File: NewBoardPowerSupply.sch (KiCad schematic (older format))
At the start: 22 parts, among them IC201 ADM7172ACPZ-4.2-R7, IC202 LT1716CS5#TRPBF, IC203 ADM7154ARDZ-3.3-R7, IC204 IRF9358PBF, U201 LM4040EIM3X-2.5_NOPB

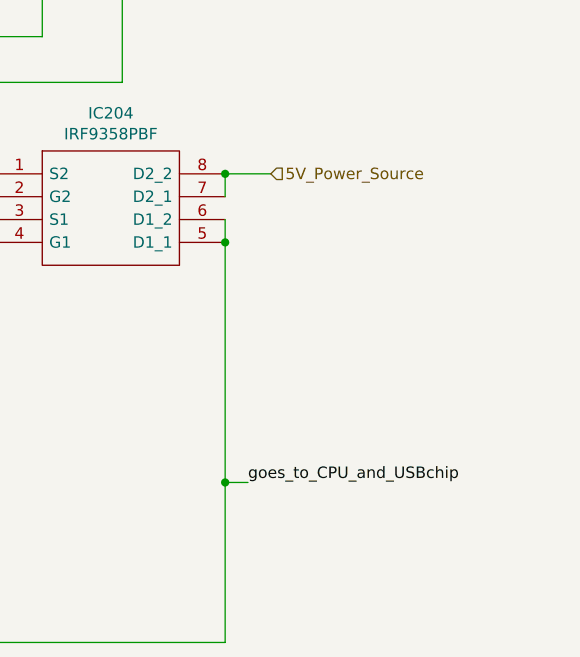
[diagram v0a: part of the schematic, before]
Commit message: added other ports
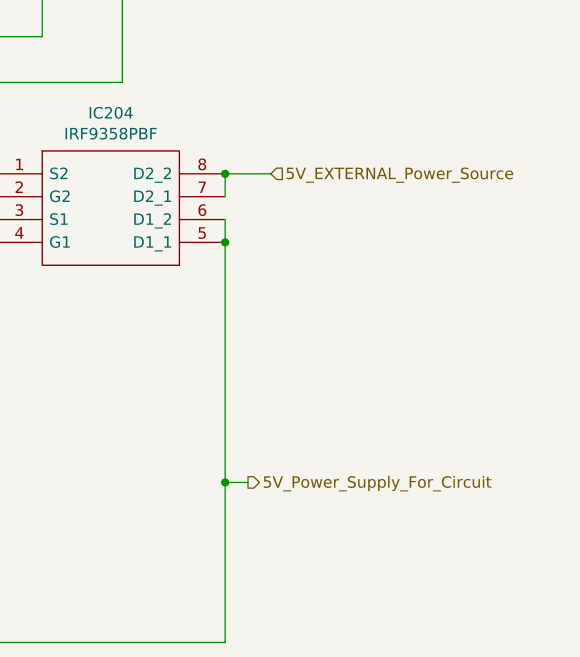
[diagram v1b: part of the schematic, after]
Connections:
- net 5V_Power_Source renamed 5V_EXTERNAL_Power_Source
- net goes_to_CPU_and_USBchip renamed 5V_Power_Supply_For_Circuit
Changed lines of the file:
@@
 	8950 2500 9150 2500
 Connection ~ 8950 2500
-Text Label 9050 3850 0    50   ~ 0
-goes_to_CPU_and_USBchip
 Wire Wire Line
 	8950 2800 8950 3850
@@
 Connection ~ 7100 4550
 Text HLabel 9150 2500 2    50   Input ~ 0
-5V_Power_Source
+5V_EXTERNAL_Power_Source
 Text HLabel 8900 5500 2    50   Output ~ 0
 3.3V_Supply
+Text HLabel 9050 3850 2    50   Output ~ 0
+5V_Power_Supply_For_Circuit
 $EndSCHEMATC

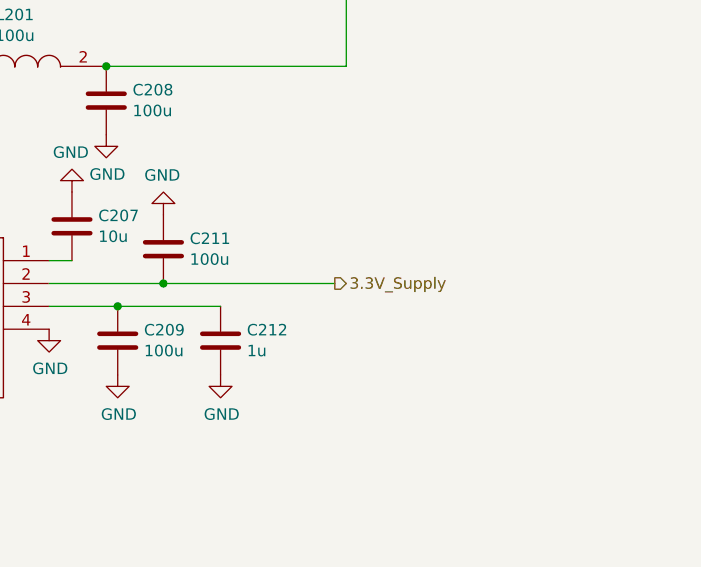
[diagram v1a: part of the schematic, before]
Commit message: added more ports
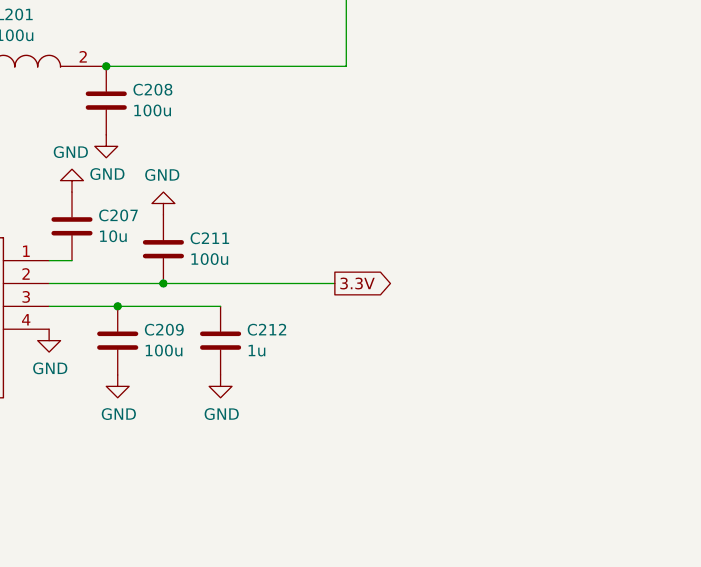
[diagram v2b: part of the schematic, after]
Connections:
- net 3.3V_Supply renamed 3.3V
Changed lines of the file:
@@
 Text HLabel 9150 2500 2    50   Input ~ 0
 5V_EXTERNAL_Power_Source
-Text HLabel 8900 5500 2    50   Output ~ 0
-3.3V_Supply
 Text HLabel 9050 3850 2    50   Output ~ 0
 5V_Power_Supply_For_Circuit
+Text GLabel 8900 5500 2    50   Output ~ 0
+3.3V
 $EndSCHEMATC

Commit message: pushing all changes and ports
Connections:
- net 4.2V_to_Power_OpAmps renamed 4.2V
- net 5V_Power_Supply_For_Circuit renamed 5.0V
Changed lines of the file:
@@
 Wire Wire Line
 	8950 2800 8950 3850
-Wire Wire Line
-	9050 3850 8950 3850
 Connection ~ 8950 3850
 Wire Wire Line
@@
 Text Notes 4950 5500 3    50   ~ 0
 4.2 Goes to Power OpAmps
-Text HLabel 4750 7000 2    50   Output ~ 0
-4.2V_to_Power_OpAmps
 Wire Wire Line
 	4650 7000 4750 7000
@@
 Text HLabel 9150 2500 2    50   Input ~ 0
 5V_EXTERNAL_Power_Source
-Text HLabel 9050 3850 2    50   Output ~ 0
-5V_Power_Supply_For_Circuit
 Text GLabel 8900 5500 2    50   Output ~ 0
 3.3V
+Text GLabel 9350 3850 2    50   Output ~ 0
+5.0V
+Wire Wire Line
+	8950 3850 9350 3850
+Text GLabel 4750 7000 2    50   Output ~ 0
+4.2V
 $EndSCHEMATC

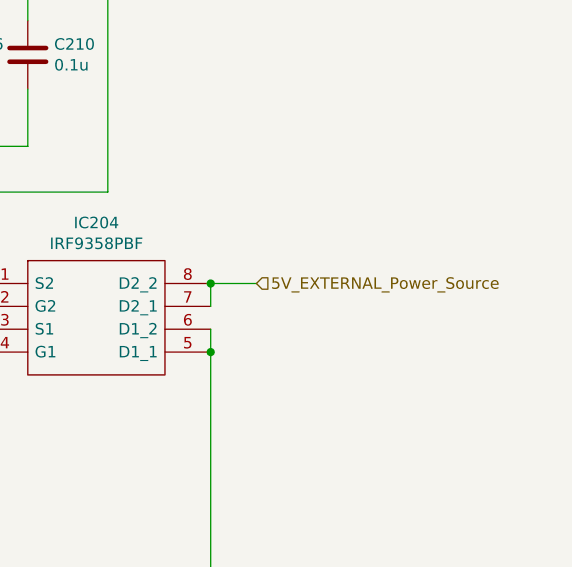
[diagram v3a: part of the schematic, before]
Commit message: replace heirarchal w/ global
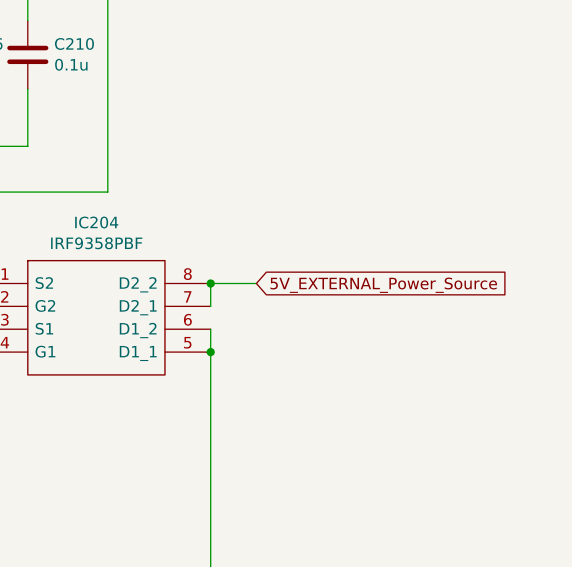
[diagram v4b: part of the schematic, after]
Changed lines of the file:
@@
 	1900 4550 7100 4550
 Connection ~ 7100 4550
-Text HLabel 9150 2500 2    50   Input ~ 0
-5V_EXTERNAL_Power_Source
 Text GLabel 8900 5500 2    50   Output ~ 0
 3.3V
@@
 Text GLabel 4750 7000 2    50   Output ~ 0
 4.2V
+Text GLabel 9150 2500 2    50   Input ~ 0
+5V_EXTERNAL_Power_Source
 $EndSCHEMATC

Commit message: did current control
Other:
- note removed: "4.2 Goes to Power OpAmps"
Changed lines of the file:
@@
 	7800 2100 7800 2500
 Connection ~ 6100 1000
-Text Notes 4950 5500 3    50   ~ 0
-4.2 Goes to Power OpAmps
 Wire Wire Line
 	4650 7000 4750 7000

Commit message: FINISHED
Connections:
- net at C204.2, IC201.5 (EN), IC201.7 (VIN_1)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: now also IC201.8 (VIN_2)
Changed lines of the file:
@@
 Connection ~ 1900 5500
 Wire Wire Line
-	1900 4550 1900 5500
+	1900 4550 1900 5400
 $Comp
 L power:GND #PWR0210
@@
 Text GLabel 9150 2500 2    50   Input ~ 0
 5V_EXTERNAL_Power_Source
+Wire Wire Line
+	2200 5400 1900 5400
+Connection ~ 1900 5400
+Wire Wire Line
+	1900 5400 1900 5500
 $EndSCHEMATC

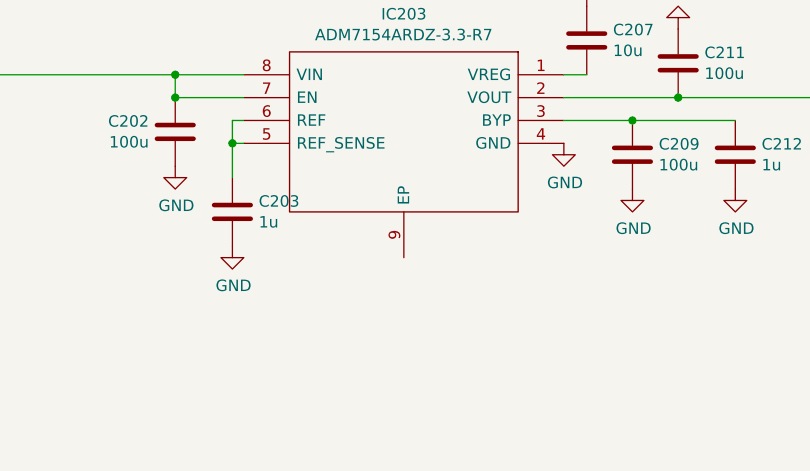
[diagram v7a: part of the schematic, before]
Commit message: grounded all other epads
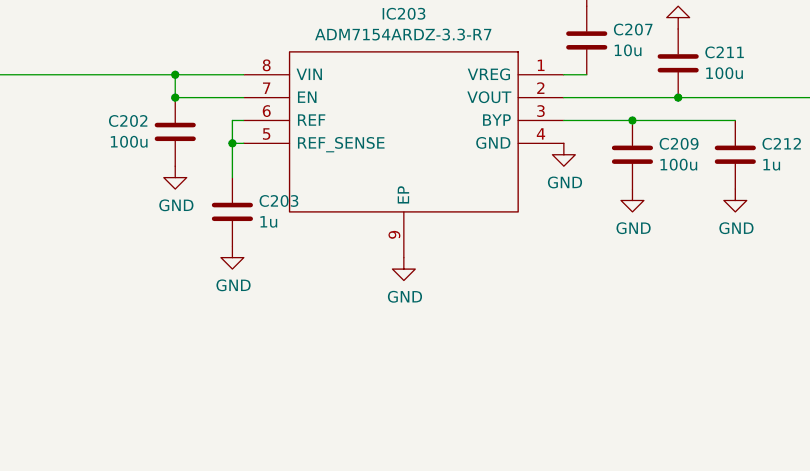
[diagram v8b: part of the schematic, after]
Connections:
- net GND: now also IC203.9 (EP)
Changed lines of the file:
@@
-$EndComp
-$Comp
-L power:GND #PWR0202
-U 1 1 60C1A400
-P 2900 6200
-F 0 "#PWR0202" H 2900 5950 50  0001 C CNN
-F 1 "GND" H 2905 6027 50  0000 C CNN
-F 2 "" H 2900 6200 50  0001 C CNN
-F 3 "" H 2900 6200 50  0001 C CNN
-	1    2900 6200
-	1    0    0    -1
 $EndComp
 $Comp
@@
 Wire Wire Line
 	1900 5400 1900 5500
+$Comp
+L power:GND #PWR0202
+U 1 1 60C1A400
+P 2900 6200
+F 0 "#PWR0202" H 2900 5950 50  0001 C CNN
+F 1 "GND" H 2905 6027 50  0000 C CNN
+F 2 "" H 2900 6200 50  0001 C CNN
+F 3 "" H 2900 6200 50  0001 C CNN
+	1    2900 6200
+	1    0    0    -1
+$EndComp
+$Comp
+L power:GND #PWR?
+U 1 1 60D4FE2D
+P 6950 6200
+F 0 "#PWR?" H 6950 5950 50  0001 C CNN
+F 1 "GND" H 6955 6027 50  0000 C CNN
+F 2 "" H 6950 6200 50  0001 C CNN
+F 3 "" H 6950 6200 50  0001 C CNN
+	1    6950 6200
+	1    0    0    -1
+$EndComp
 $EndSCHEMATC
